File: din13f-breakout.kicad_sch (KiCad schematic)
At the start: 28 parts, among them J1 SCART-F, J4 SDD-130J, U1 LM1881, U2 74LS00, U3 MCP6499, X1 USB-B1HSB6

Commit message: Fully popped
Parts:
- added TP1, TP2, TP3, TP4: TestPoint, TestPoint:TestPoint_Loop_D2.50mm_Drill1.0mm, symbol Connector:TestPoint
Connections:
- net HSync is gone; now on net Hsync: J4.9
- net +5V: now also TP1.1
- net GND: now also TP2.1
- net GREEN: now also TP4.1
- net SCART_Green: now also TP3.1
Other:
- note removed: "TODO: 4.3k seems hard to find, let's monkey with this math"
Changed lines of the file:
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@@
   (junction (at 60.325 186.69) (diameter 0) (color 0 0 0 0)
   )
+  (junction (at 58.42 162.56) (diameter 0) (color 0 0 0 0)
+  )
   (junction (at 213.995 47.625) (diameter 0) (color 0 0 0 0)
+  )
+  (junction (at 89.535 165.1) (diameter 0) (color 0 0 0 0)
   )
   (junction (at 60.325 150.495) (diameter 0) (color 0 0 0 0)
@@
     (stroke (width 0) (type default))
   )
+  (wire (pts (xy 78.105 147.955) (xy 92.71 147.955))
+    (stroke (width 0) (type default))
+  )
   (wire (pts (xy 88.9 39.37) (xy 88.9 40.005))
     (stroke (width 0) (type default))
@@
     (stroke (width 0) (type default))
   )
+  (wire (pts (xy 196.215 149.86) (xy 200.025 149.86))
+    (stroke (width 0) (type default))
+  )
   (wire (pts (xy 56.515 104.775) (xy 77.47 104.775))
     (stroke (width 0) (type default))
   )
+  (wire (pts (xy 58.42 162.56) (xy 62.865 162.56))
+    (stroke (width 0) (type default))
+  )
   (wire (pts (xy 213.995 50.165) (xy 213.995 47.625))
     (stroke (width 0) (type default))
@@
     (stroke (width 0) (type default))
   )
-  (wire (pts (xy 56.515 162.56) (xy 62.865 162.56))
+  (wire (pts (xy 56.515 162.56) (xy 58.42 162.56))
     (stroke (width 0) (type default))
   )
@@
     (stroke (width 0) (type default))
   )
-  (wire (pts (xy 78.105 147.955) (xy 92.71 147.955))
+  (wire (pts (xy 89.535 165.1) (xy 92.71 165.1))
     (stroke (width 0) (type default))
   )
@@
     (stroke (width 0) (type default))
   )
+  (wire (pts (xy 200.025 149.86) (xy 200.025 143.51))
+    (stroke (width 0) (type default))
+  )
   (wire (pts (xy 81.915 40.005) (xy 75.565 40.005))
     (stroke (width 0) (type default))
@@
     (stroke (width 0) (type default))
   )
+  (wire (pts (xy 56.515 145.415) (xy 62.865 145.415))
+    (stroke (width 0) (type default))
+  )
   (wire (pts (xy 213.995 47.625) (xy 213.995 45.085))
     (stroke (width 0) (type default))
@@
     (stroke (width 0) (type default))
   )
-  (wire (pts (xy 56.515 145.415) (xy 62.865 145.415))
-    (stroke (width 0) (type default))
-  )
-  (wire (pts (xy 78.105 165.1) (xy 92.71 165.1))
+  (wire (pts (xy 78.105 165.1) (xy 89.535 165.1))
     (stroke (width 0) (type default))
   )
@@
     (effects (font (size 1.27 1.27)) (justify right bottom))
   )
-  (text "TODO: 4.3k seems hard to find, let's monkey with this math"
-    (at 48.26 137.16 0)
-    (effects (font (size 1.27 1.27)) (justify left bottom))
-  )
   (text "Mixing audio together\n(TODO: exact values)" (at 147.32 89.535 0)
     (effects (font (size 1.27 1.27)) (justify left bottom))
@@
     (effects (font (size 1.27 1.27)) (justify right bottom))
   )
-  (label "HSync" (at 245.745 97.155 180) (fields_autoplaced)
+  (label "Hsync" (at 245.745 97.155 180) (fields_autoplaced)
     (effects (font (size 1.27 1.27)) (justify right bottom))
   )
@@
     )
   )
+  (symbol (lib_id "Connector:TestPoint") (at 186.69 143.51 0) (unit 1)
+    (in_bom yes) (on_board yes) (dnp no) (fields_autoplaced)
+    (property "Reference" "TP2" (at 189.23 140.208 0)
+      (effects (font (size 1.27 1.27)) (justify left))
+    )
+    (property "Value" "TestPoint" (at 188.595 141.478 0)
+      (effects (font (size 1.27 1.27)) (justify left) hide)
+    )
+    (property "Footprint" "TestPoint:TestPoint_Loop_D2.50mm_Drill1.0mm" (at 191.77 143.51 0)
+      (effects (font (size 1.27 1.27)) hide)
+    )
+    (property "Datasheet" "~" (at 191.77 143.51 0)
+      (effects (font (size 1.27 1.27)) hide)
+    )
+    (pin "1")
+    (instances
+      (project "din13f-breakout"
+        (path "/f613f4f9-4f4a-4ef5-a528-9642b0c971e3"
+          (reference "TP2") (unit 1)
+        )
+      )
+    )
+  )
   (symbol (lib_id "Jumper:Jumper_2_Bridged") (at 113.03 112.395 0) (unit 1)
     (in_bom yes) (on_board yes) (dnp no) (fields_autoplaced)
@@
     )
   )
+  (symbol (lib_id "power:+5V") (at 196.215 149.86 0) (unit 1)
+    (in_bom yes) (on_board yes) (dnp no) (fields_autoplaced)
+    (property "Reference" "#PWR020" (at 196.215 153.67 0)
+      (effects (font (size 1.27 1.27)) hide)
+    )
+    (property "Value" "+5V" (at 196.215 144.78 0)
+      (effects (font (size 1.27 1.27)))
+    )
+    (property "Footprint" "" (at 196.215 149.86 0)
+      (effects (font (size 1.27 1.27)) hide)
+    )
+    (property "Datasheet" "" (at 196.215 149.86 0)
+      (effects (font (size 1.27 1.27)) hide)
+    )
+    (pin "1")
+    (instances
+      (project "din13f-breakout"
+        (path "/f613f4f9-4f4a-4ef5-a528-9642b0c971e3"
+          (reference "#PWR020") (unit 1)
+        )
+      )
+    )
+  )
   (symbol (lib_id "Device:R_Small_US") (at 155.575 107.95 90) (unit 1)
     (in_bom yes) (on_board yes) (dnp no) (fields_autoplaced)
@@
         (path "/f613f4f9-4f4a-4ef5-a528-9642b0c971e3"
           (reference "R3") (unit 1)
+        )
+      )
+    )
+  )
+  (symbol (lib_id "Connector:TestPoint") (at 58.42 162.56 0) (unit 1)
+    (in_bom yes) (on_board yes) (dnp no) (fields_autoplaced)
+    (property "Reference" "TP3" (at 60.325 159.258 0)
+      (effects (font (size 1.27 1.27)) (justify left))
+    )
+    (property "Value" "TestPoint" (at 60.325 160.528 0)
+      (effects (font (size 1.27 1.27)) (justify left) hide)
+    )
+    (property "Footprint" "TestPoint:TestPoint_Loop_D2.50mm_Drill1.0mm" (at 63.5 162.56 0)
+      (effects (font (size 1.27 1.27)) hide)
+    )
+    (property "Datasheet" "~" (at 63.5 162.56 0)
+      (effects (font (size 1.27 1.27)) hide)
+    )
+    (pin "1")
+    (instances
+      (project "din13f-breakout"
+        (path "/f613f4f9-4f4a-4ef5-a528-9642b0c971e3"
+          (reference "TP3") (unit 1)
         )
       )
@@
         (path "/f613f4f9-4f4a-4ef5-a528-9642b0c971e3"
           (reference "JP1") (unit 1)
+        )
+      )
+    )
+  )
+  (symbol (lib_id "Connector:TestPoint") (at 200.025 143.51 0) (unit 1)
+    (in_bom yes) (on_board yes) (dnp no) (fields_autoplaced)
+    (property "Reference" "TP1" (at 201.93 140.208 0)
+      (effects (font (size 1.27 1.27)) (justify left))
+    )
+    (property "Value" "TestPoint" (at 201.93 141.478 0)
+      (effects (font (size 1.27 1.27)) (justify left) hide)
+    )
+    (property "Footprint" "TestPoint:TestPoint_Loop_D2.50mm_Drill1.0mm" (at 205.105 143.51 0)
+      (effects (font (size 1.27 1.27)) hide)
+    )
+    (property "Datasheet" "~" (at 205.105 143.51 0)
+      (effects (font (size 1.27 1.27)) hide)
+    )
+    (pin "1")
+    (instances
+      (project "din13f-breakout"
+        (path "/f613f4f9-4f4a-4ef5-a528-9642b0c971e3"
+          (reference "TP1") (unit 1)
         )
       )
@@
         (path "/f613f4f9-4f4a-4ef5-a528-9642b0c971e3"
           (reference "R12") (unit 1)
+        )
+      )
+    )
+  )
+  (symbol (lib_id "power:GND") (at 186.69 143.51 0) (unit 1)
+    (in_bom yes) (on_board yes) (dnp no) (fields_autoplaced)
+    (property "Reference" "#PWR019" (at 186.69 149.86 0)
+      (effects (font (size 1.27 1.27)) hide)
+    )
+    (property "Value" "GND" (at 186.69 148.59 0)
+      (effects (font (size 1.27 1.27)))
+    )
+    (property "Footprint" "" (at 186.69 143.51 0)
+      (effects (font (size 1.27 1.27)) hide)
+    )
+    (property "Datasheet" "" (at 186.69 143.51 0)
+      (effects (font (size 1.27 1.27)) hide)
+    )
+    (pin "1")
+    (instances
+      (project "din13f-breakout"
+        (path "/f613f4f9-4f4a-4ef5-a528-9642b0c971e3"
+          (reference "#PWR019") (unit 1)
         )
       )
@@
         )
       )
+    )
+  )
+  (symbol (lib_id "Connector:TestPoint") (at 89.535 165.1 0) (unit 1)
+    (in_bom yes) (on_board yes) (dnp no) (fields_autoplaced)
+    (property "Reference" "TP4" (at 91.44 161.798 0)
+      (effects (font (size 1.27 1.27)) (justify left))
+    )
+    (property "Value" "TestPoint" (at 91.44 163.068 0)
+      (effects (font (size 1.27 1.27)) (justify left) hide)
+    )
+    (property "Footprint" "TestPoint:TestPoint_Loop_D2.50mm_Drill1.0mm" (at 94.615 165.1 0)
+      (effects (font (size 1.27 1.27)) hide)
+    )
+    (property "Datasheet" "~" (at 94.615 165.1 0)
+      (effects (font (size 1.27 1.27)) hide)
+    )
+    (pin "1")
+    (instances
+      (project "din13f-breakout"
+        (path "/f613f4f9-4f4a-4ef5-a528-9642b0c971e3"
+          (reference "TP4") (unit 1)
+        )
+      )

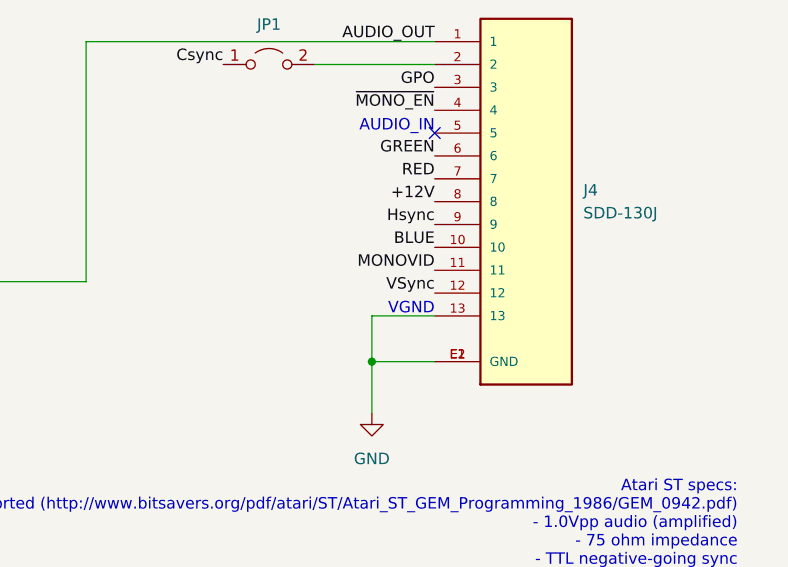
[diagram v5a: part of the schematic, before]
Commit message: Fix missing Vsync
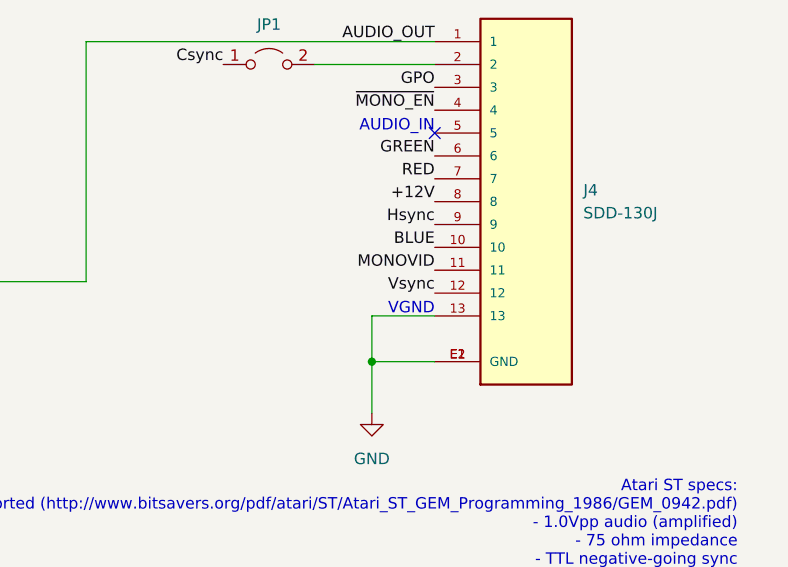
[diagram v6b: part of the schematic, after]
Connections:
- net VSync is gone; now on net Vsync: J4.12
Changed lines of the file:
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@@
     (effects (font (size 1.27 1.27)) (justify right bottom))
   )
-  (label "VSync" (at 245.745 104.775 180) (fields_autoplaced)
+  (label "Vsync" (at 245.745 104.775 180) (fields_autoplaced)
     (effects (font (size 1.27 1.27)) (justify right bottom))
   )
